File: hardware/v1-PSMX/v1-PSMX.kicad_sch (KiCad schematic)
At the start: 9 parts, among them IC1 MAX98357AETE+T, J1 USB_B_Micro, SW1 SW_Push_PRG_RST, SW2 SW_Push_RST, U1 ESP32-S3-WROOM-1

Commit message: Init work on hardware schematic
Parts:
- removed SW1: SW_Push_PRG_RST, symbol Switch:SW_Push
- removed SW2: SW_Push_RST, symbol Switch:SW_Push
- added C? (x4): 0.1uF, symbol Device:C
- added C? (x4): 10uF, symbol Device:C
- added IC?: MAX98357AETE+T (R), QFN50P300X300X80-17N, symbol MAX98357AETE+T:MAX98357AETE+T
- added J?: Serial_Breakout, symbol Connector_Generic:Conn_01x06
- added J?: Right_Speaker, symbol Connector_Generic:Conn_01x02
- added J?: Left_Speaker, symbol Connector_Generic:Conn_01x02
- added R? (x2): GAIN SELECT, Connector_Wire:SolderWirePad_1x01_SMD_1x2mm, symbol Device:R_US
- added R? (x3): 270ohm, symbol Device:R_US
- added R?: 220k_ohm, symbol Device:R_US
- added SW?: RST_TO_PRGM, symbol Switch:SW_Push
- added SW?: RESET, symbol Switch:SW_Push
- C?: value Capacitor_2uF -> 2uF
- IC1: value MAX98357AETE+T -> MAX98357AETE+T (L)
- R?: value R_10k_ohm -> 10k_ohm
- U?: footprint (none) -> Package_TO_SOT_SMD:TO-252-2
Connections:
- net +3.3V: now also LED1.1 (COMMON_ANODE), U?.2 (VO), C?.1, C?.1, J?.1 (Pin_1)
- net +5V: now also IC1.7 (VDD_1), IC1.8 (VDD_2), U?.3 (VI), C?.1, C?.1, C?.1, C?.1, C?.1, C?.1, IC?.7 (VDD_1), IC?.8 (VDD_2), R?.1
- net GND: now also IC1.11 (GND_2), IC1.15 (GND_3), IC1.17 (THERMAL_PAD), IC1.3 (GND_1), U?.1 (GND), C?.2, C?.2, C?.2, C?.2, C?.2, C?.2, C?.2, C?.2, IC?.11 (GND_2), IC?.15 (GND_3), IC?.17 (THERMAL_PAD), IC?.3 (GND_1), J?.2 (Pin_2), R?.1, SW?.1, SW?.2
- net RESET: now reaches C?.1, R?.2, U1.3 (EN)
- net RESET: now also J?.4 (Pin_4), SW?.2
- net RST_TO_PRGM: now reaches C?.2, U1.27 (GPIO0/BOOT)
- net RST_TO_PRGM: now also J?.3 (Pin_3), SW?.1
- net at LED1.2 (CATHODE_BLUE): now also R?.2
- net at LED1.3 (CATHODE_GREEN): now also R?.2
- net at LED1.4 (CATHODE_RED): now also R?.2
- net at IC1.1 (DIN): now also U1.20 (GPIO12/TOUCH12/ADC2_CH1/FSPICLK/FSPIIO6/SUBSPICLK), IC?.1 (DIN)
- net at IC1.10 (OUTN): now also J?.1 (Pin_1)
- net at IC1.14 (LRCLK): now also U1.22 (GPIO14/TOUCH14/ADC2_CH3/FSPIWP/FSPIDQS/SUBSPIWP), IC?.14 (LRCLK)
- net at IC1.16 (BCLK): now also U1.21 (GPIO13/TOUCH13/ADC2_CH2/FSPIQ/FSPIIO7/SUBSPIQ), IC?.16 (BCLK)
- net at IC1.2 (GAIN_SLOT): now also IC?.2 (GAIN_SLOT), R?.2, R?.2
- net at IC1.4 (~{SD_MODE}): now also U1.11 (GPIO18/U1RXD/ADC2_CH7/CLK_OUT3), R?.2
- net at IC1.9 (OUTP): now also J?.2 (Pin_2)
- net at U1.36 (U0RXD/GPIO44/CLK_OUT2): now also J?.5 (Pin_5)
- net at U1.37 (U0TXD/GPIO43/CLK_OUT1): now also J?.6 (Pin_6)
- new net: IC?.10 (OUTN), J?.1 (Pin_1)
- new net: IC?.4 (~{SD_MODE}), R?.1
- new net: IC?.9 (OUTP), J?.2 (Pin_2)
- no-connect marks 0 -> 9
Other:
- note added: "RESET"
- note added: "RST_TO_PRGM"
- note added: "RX (MASTER)"
- note added: "TX (MASTER)"
- moved on the sheet: C?, IC1, J1, LED1, R?, U1, U?

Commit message: Init work on schematic
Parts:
- removed C?: 0.1uF, symbol Device:C
- removed C?: 10uF, symbol Device:C
- removed J?: Right_Speaker, symbol Connector_Generic:Conn_01x02
- removed R?: GAIN SELECT, Connector_Wire:SolderWirePad_1x01_SMD_1x2mm, symbol Device:R_US
- removed R? (x3): 270ohm, symbol Device:R_US
- added C? (x4): 0.1uF, symbol Device:C
- added C? (x2): 10uF, symbol Device:C
- added J?: +5V, symbol Connector_Generic:Conn_01x02
- added J?: Right_Speaker, symbol Connector_Generic:Conn_01x02
- added R? (x3): 270ohm, symbol Device:R_US
- added R?: GAIN SELECT, Connector_Wire:SolderWirePad_1x01_SMD_1x2mm, symbol Device:R_US
- added VR?: P110KH1-0F15BR10K, P110KH10F15BR10K, symbol P110KH1-0F15BR10K:P110KH1-0F15BR10K
- added VR?: PTA3043-2015DPB104, PTA30432015DPB104, symbol PTA3043-2015DPB104:PTA3043-2015DPB104
- J?: footprint (none) -> Connector_PinHeader_2.54mm:PinHeader_1x06_P2.54mm_Vertical
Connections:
- net +3.3V: now also C?.1, C?.1, VR?.1 (CCW), VR?.3 (CW); no longer J?.1 (Pin_1)
- net +5V: now also J?.1 (Pin_1), C?.1, C?.1, J?.1 (Pin_1), R?.1
- net GND: now also SW?.2, C?.2, C?.2, C?.2, C?.2, C?.2, C?.2, J?.2 (Pin_2), VR?.1 (CCW), VR?.3 (CW), VR?.4 (DUMMY), VR?.MH1, VR?.MH1, VR?.MH2, VR?.MH2, VR?.MH3, VR?.MH4; no longer SW?.1
- net RESET: now also SW?.1; no longer SW?.2
- net DIN_GPIO12: now reaches IC1.1 (DIN), IC?.1 (DIN), U1.20 (GPIO12/TOUCH12/ADC2_CH1/FSPICLK/FSPIIO6/SUBSPICLK)
- net at IC?.10 (OUTN): now also J?.2 (Pin_2)
- net LRCLK_GPIO14: now reaches IC1.14 (LRCLK), IC?.14 (LRCLK), U1.22 (GPIO14/TOUCH14/ADC2_CH3/FSPIWP/FSPIDQS/SUBSPIWP)
- net BCLK_GPIO13: now reaches IC1.16 (BCLK), IC?.16 (BCLK), U1.21 (GPIO13/TOUCH13/ADC2_CH2/FSPIQ/FSPIIO7/SUBSPIQ)
- net GAIN_SLOT: now reaches IC1.2 (GAIN_SLOT), IC?.2 (GAIN_SLOT), R?.2
- net GAIN_SLOT: now also R?.2
- net at IC?.9 (OUTP): now also J?.1 (Pin_1)
- net U0RXD_TX: now reaches J?.5 (Pin_5), U1.36 (U0RXD/GPIO44/CLK_OUT2)
- net U0TXD_RX: now reaches J?.6 (Pin_6), U1.37 (U0TXD/GPIO43/CLK_OUT1)
- net at LED1.2 (CATHODE_BLUE): now also R?.2
- net at LED1.3 (CATHODE_GREEN): now also R?.2
- net at LED1.4 (CATHODE_RED): now also R?.2
- net GPIO19_USB_D-: now reaches J1.2 (D-), U1.13 (GPIO19/U1RTS/ADC2_CH8/CLK_OUT2/USB_D-)
- net GPIO20_USB_D+: now reaches J1.3 (D+), U1.14 (GPIO20/U1CTS/ADC2_CH9/CLK_OUT1/USB_D+)
- net at IC1.10 (OUTN): now also J?.2 (Pin_2); no longer J?.1 (Pin_1)
- net SD_MODE_GPIO11: now reaches IC1.4 (~{SD_MODE}), R?.2
- net SD_MODE_GPIO11: now also U1.19 (GPIO11/TOUCH11/ADC2_CH0/FSPID/FSPIIO5/SUBSPID); no longer U1.11 (GPIO18/U1RXD/ADC2_CH7/CLK_OUT3)
- net at IC1.9 (OUTP): now also J?.1 (Pin_1); no longer J?.2 (Pin_2)
- net S_POT_GPIO9: now reaches U1.17 (GPIO9/TOUCH9/ADC1_CH8/FSPIHD/SUBSPIHD)
- net S_POT_GPIO9: now also C?.1, VR?.2 (WIPER)
- net V_POT_GPIO10: now reaches U1.18 (GPIO10/TOUCH10/ADC1_CH9/FSPICS0/FSPIIO4/SUBSPICS0)
- net V_POT_GPIO10: now also C?.1, VR?.2 (WIPER)
- net LED_RED_GPIO4: now reaches U1.4 (GPIO4/TOUCH4/ADC1_CH3)
- net LED_RED_GPIO4: now also R?.1
- net LED_GREEN_GPIO5: now reaches U1.5 (GPIO5/TOUCH5/ADC1_CH4)
- net LED_GREEN_GPIO5: now also R?.1
- net LED_BLUE_GPIO6: now reaches U1.6 (GPIO6/TOUCH6/ADC1_CH5)
- net LED_BLUE_GPIO6: now also R?.1
- no-connect marks 9 -> 12
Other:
- note added: "5V"
- note added: "GAIN SELECT"
- note added: "LEFT DAC & AMP"
- note added: "RESET & RESET TO PROGRAM BUTTONS"
- note added: "RGB LED"
- note added: "RIGHT DAC & AMP"
- note added: "SERIAL BREAKOUT"
- note added: "STATION POT"
- note added: "USB PORT"
- note added: "VOLTAGE REGULATOR (5V->3.3V)"
- note added: "VOLUME POT"
- note removed: "RESET"
- note removed: "RST_TO_PRGM"
- moved on the sheet: C?, IC1, IC?, J1, J?, LED1, R?, SW?, U1, U?

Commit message: Improvements to schematic
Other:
- note added: "SPEAKER OUT"
- moved on the sheet: C?, IC1, J?, LED1, R?, U1

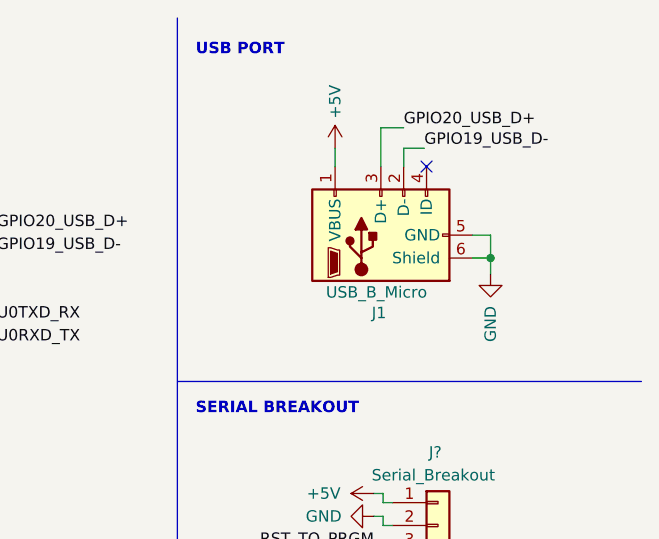
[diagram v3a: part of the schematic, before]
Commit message: Added ESD protection to USB connection
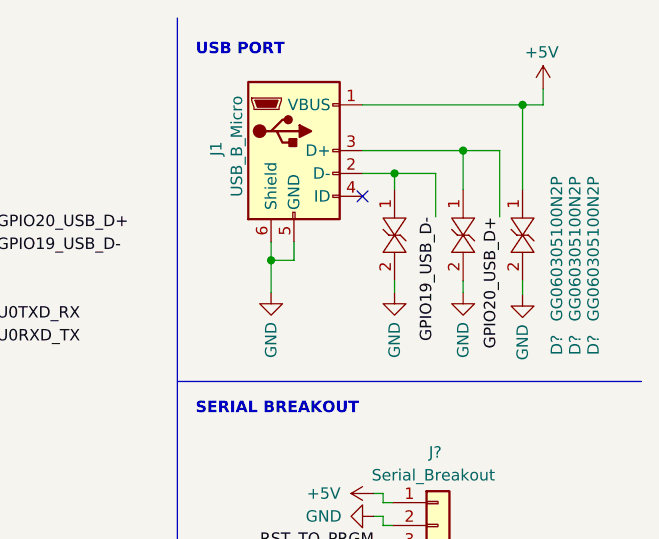
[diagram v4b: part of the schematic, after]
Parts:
- added D? (x3): GG060305100N2P, DIONC1608X70N, symbol my-symbols:GG060305100N2P
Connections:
- net +5V: now also D?.1
- net GND: now also D?.2, D?.2, D?.2
- net GPIO19_USB_D-: now also D?.1
- net GPIO20_USB_D+: now also D?.1
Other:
- moved on the sheet: J1

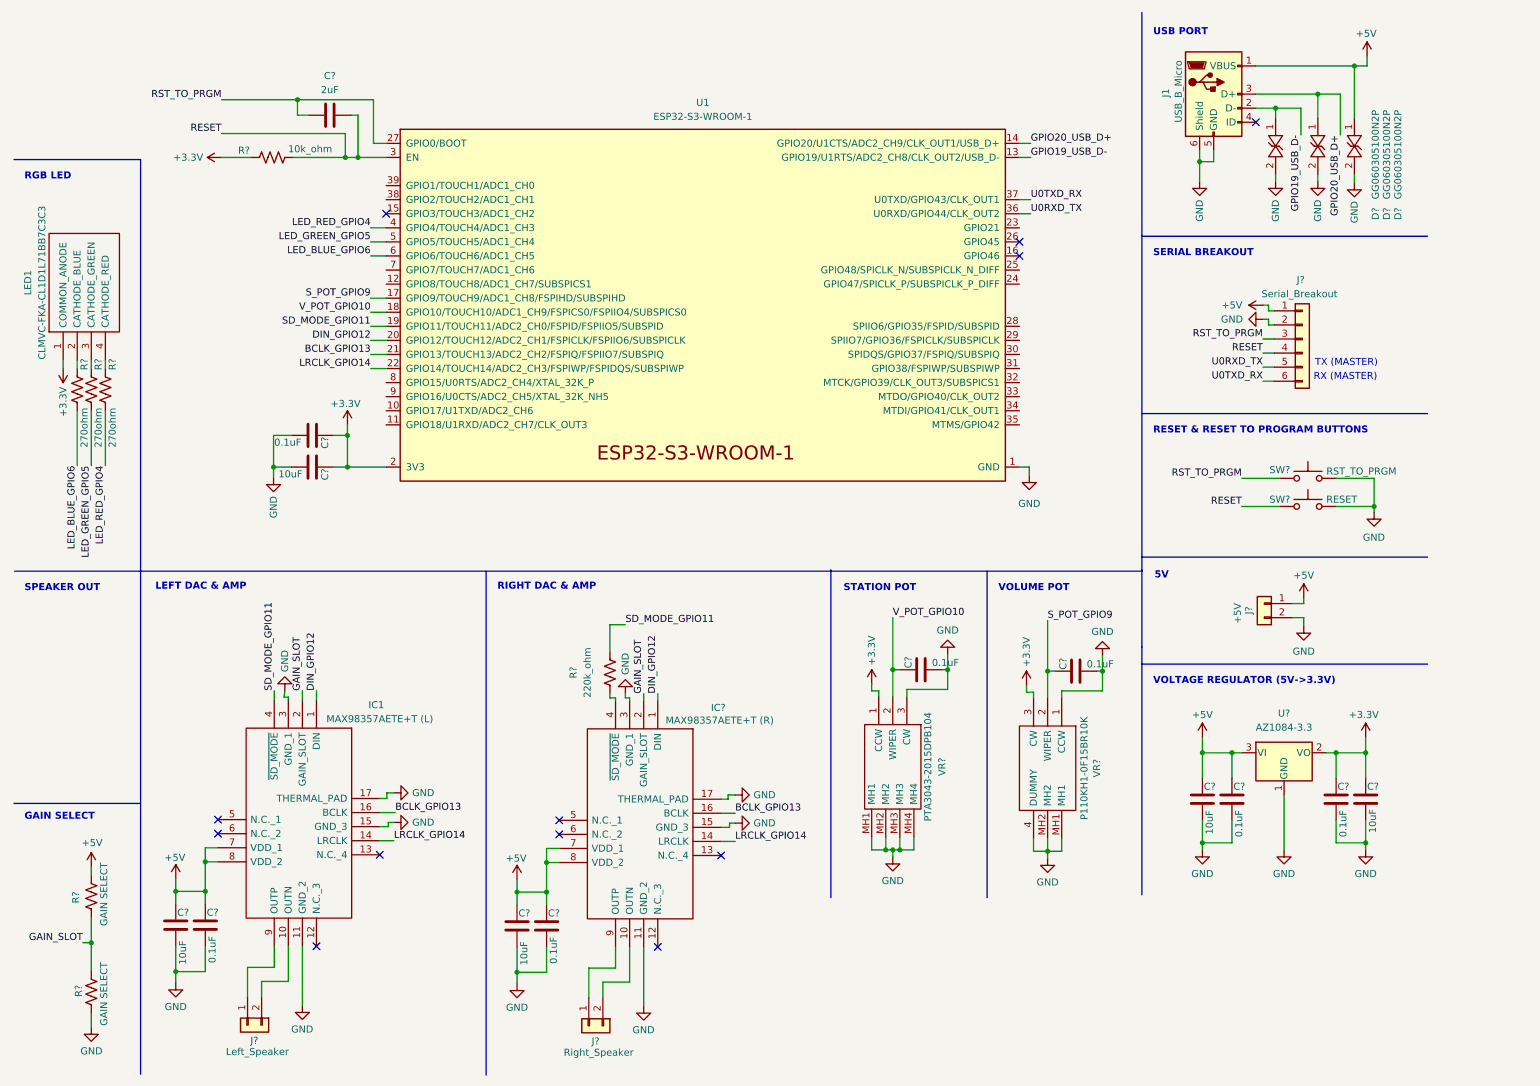
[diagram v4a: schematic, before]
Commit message: Completed Init work on schematic
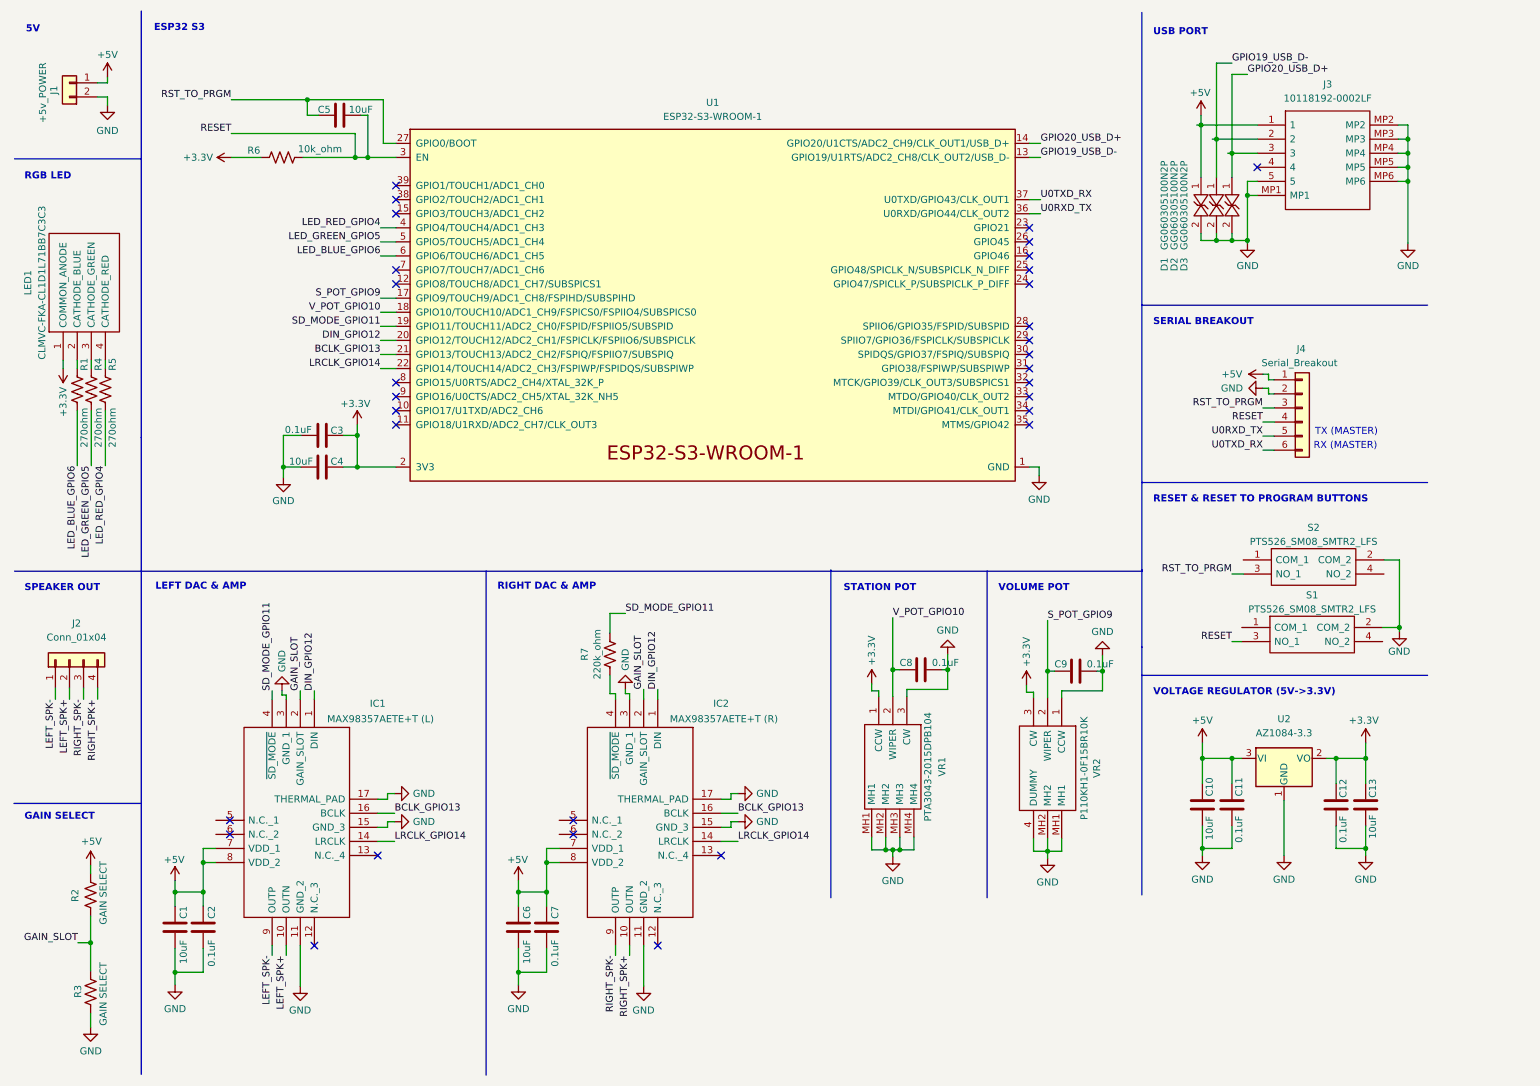
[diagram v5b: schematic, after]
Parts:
- removed C?: 0.1uF, symbol Device:C
- removed C?: 10uF, symbol Device:C
- removed IC?: MAX98357AETE+T (R), QFN50P300X300X80-17N, symbol MAX98357AETE+T:MAX98357AETE+T
- removed J1: USB_B_Micro, symbol Connector:USB_B_Micro
- removed J?: Right_Speaker, symbol Connector_Generic:Conn_01x02
- removed J?: Left_Speaker, symbol Connector_Generic:Conn_01x02
- removed SW?: RST_TO_PRGM, symbol Switch:SW_Push
- removed SW?: RESET, symbol Switch:SW_Push
- added C6: 10uF, Capacitor_SMD:C_0805_2012Metric, symbol Device:C
- added C7: 0.1uF, Capacitor_SMD:C_0805_2012Metric, symbol Device:C
- added IC2: MAX98357AETE+T (R), MAX98357AETE+T:QFN50P300X300X80-17N, symbol MAX98357AETE+T:MAX98357AETE+T
- added J2: Conn_01x04, Connector_JST:JST_XH_B4B-XH-A_1x04_P2.50mm_Vertical, symbol Connector_Generic:Conn_01x04
- added J3: 10118192-0002LF, my-footprints:101181920002LF, symbol my-symbols-3:10118192-0002LF
- added S1, S2: PTS526_SM08_SMTR2_LFS, my-footprints:PTS526SM08SMTR2LFS, symbol my-symbols-2:PTS526_SM08_SMTR2_LFS
- C1, C10, C11, C12, C13, C2, C3, C4, C8, C9: renamed from C?; footprint (none) -> Capacitor_SMD:C_0805_2012Metric
- C5: renamed from C?; value 2uF -> 10uF; footprint (none) -> Capacitor_SMD:C_0805_2012Metric
- D1, D2, D3: renamed from D?; footprint DIONC1608X70N -> my-footprints:DIONC1608X70N
- IC1: footprint QFN50P300X300X80-17N -> MAX98357AETE+T:QFN50P300X300X80-17N
- J1: renamed from J?; value +5V -> +5v_POWER; footprint (none) -> my-footprints:CUSTOM_5V_SOLDER_PADS
- LED1: footprint CLMVCFKACL1D1L71BB7C3C3 -> CLMVC-FKA-CL1D1L71BB7C3C3:CLMVCFKACL1D1L71BB7C3C3
- R1, R4, R5, R6, R7: renamed from R?; footprint (none) -> Resistor_SMD:R_1206_3216Metric
- VR1: renamed from VR?; footprint PTA30432015DPB104 -> my-footprints:PTA30432015DPB104
- VR2: renamed from VR?; footprint P110KH10F15BR10K -> my-footprints:P110KH10F15BR10K
- gave numbers to parts that had none: 4
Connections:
- net +5V: now also C6.1, C7.1, IC2.7 (VDD_1), IC2.8 (VDD_2), J3.1
- net BCLK_GPIO13: now also IC2.16 (BCLK)
- net DIN_GPIO12: now also IC2.1 (DIN)
- net GAIN_SLOT: now also IC2.2 (GAIN_SLOT)
- net GND: now also C6.2, C7.2, IC2.11 (GND_2), IC2.15 (GND_3), IC2.17 (THERMAL_PAD), IC2.3 (GND_1), J3.5, J3.MP1, J3.MP2, J3.MP3, J3.MP4, J3.MP5, J3.MP6, S1.2 (COM_2), S2.2 (COM_2)
- net GPIO19_USB_D-: now also J3.2
- net GPIO20_USB_D+: now also J3.3
- net LRCLK_GPIO14: now also IC2.14 (LRCLK)
- net RESET: now also S1.3 (NO_1)
- net RST_TO_PRGM: now also S2.3 (NO_1)
- net at R7.1: now also IC2.4 (~{SD_MODE})
- net LEFT_SPK+: now reaches IC1.10 (OUTN)
- net LEFT_SPK+: now also J2.2 (Pin_2)
- net LEFT_SPK-: now reaches IC1.9 (OUTP)
- net LEFT_SPK-: now also J2.1 (Pin_1)
- new net RIGHT_SPK+: IC2.10 (OUTN), J2.4 (Pin_4)
- new net RIGHT_SPK-: IC2.9 (OUTP), J2.3 (Pin_3)
- no-connect marks 12 -> 31
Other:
- note added: "ESP32 S3"
- moved on the sheet: C10, C11, C12, C13, C2, C3, C4, C5, D1, D2, D3, J1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

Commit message: init work on pcb
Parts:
- R2: value GAIN SELECT -> GAIN SELECT HIGH; footprint Connector_Wire:SolderWirePad_1x01_SMD_1x2mm -> Resistor_SMD:R_1206_3216Metric
- R3: value GAIN SELECT -> GAIN SELECT LOW; footprint Connector_Wire:SolderWirePad_1x01_SMD_1x2mm -> Resistor_SMD:R_1206_3216Metric
- U1: footprint Espressif:ESP32-S3-WROOM-1 -> Espressif:ESP32-S3-WROOM-1U
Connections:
- net S_POT_GPIO9 renamed S_POT_GPIO10
- net S_POT_GPIO10: now also U1.18 (GPIO10/TOUCH10/ADC1_CH9/FSPICS0/FSPIIO4/SUBSPICS0); no longer U1.17 (GPIO9/TOUCH9/ADC1_CH8/FSPIHD/SUBSPIHD)
- net V_POT_GPIO10 renamed V_POT_GPIO09
- net V_POT_GPIO09: now also U1.17 (GPIO9/TOUCH9/ADC1_CH8/FSPIHD/SUBSPIHD); no longer U1.18 (GPIO10/TOUCH10/ADC1_CH9/FSPICS0/FSPIIO4/SUBSPICS0)
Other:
- moved on the sheet: J2, R2, R3
